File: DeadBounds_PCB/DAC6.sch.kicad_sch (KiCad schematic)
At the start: 0 parts

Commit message: Added 6-bit DAC
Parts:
- added LS1: Speaker, symbol Device:Speaker
- added R1, R2, R3, R4, R5: 12k, symbol Device:R_US
- added R10, R6, R7, R8, R9: 1.5k, symbol Device:R_US
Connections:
- new net: LS1.1, R1.2, R10.2, R3.2, R4.2, R5.2, R6.2, R8.2, R9.2
- new net: R6.1, R7.2
- new net: R1.1, R2.2
- new net DAC6_0: R2.1
- new net DAC6_1: R3.1
- new net DAC6_2: R4.1, R5.1
- new net DAC6_3: R7.1
- new net DAC6_4: R8.1
- new net DAC6_5: R10.1, R9.1
- new net GND: LS1.2

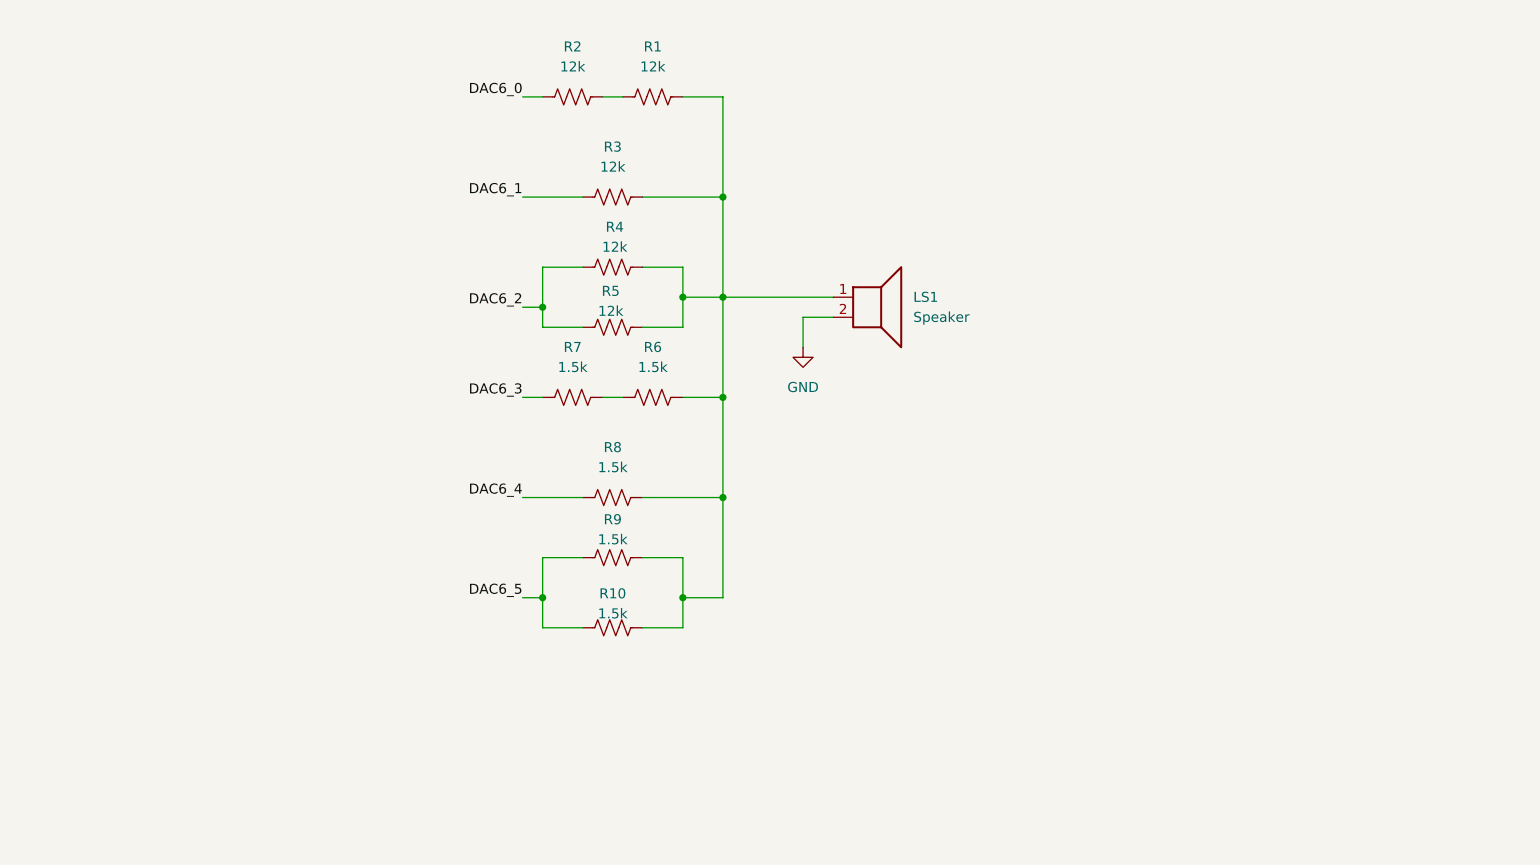
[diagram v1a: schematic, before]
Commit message: Finished schematics, assigned/made footprints except for resistors
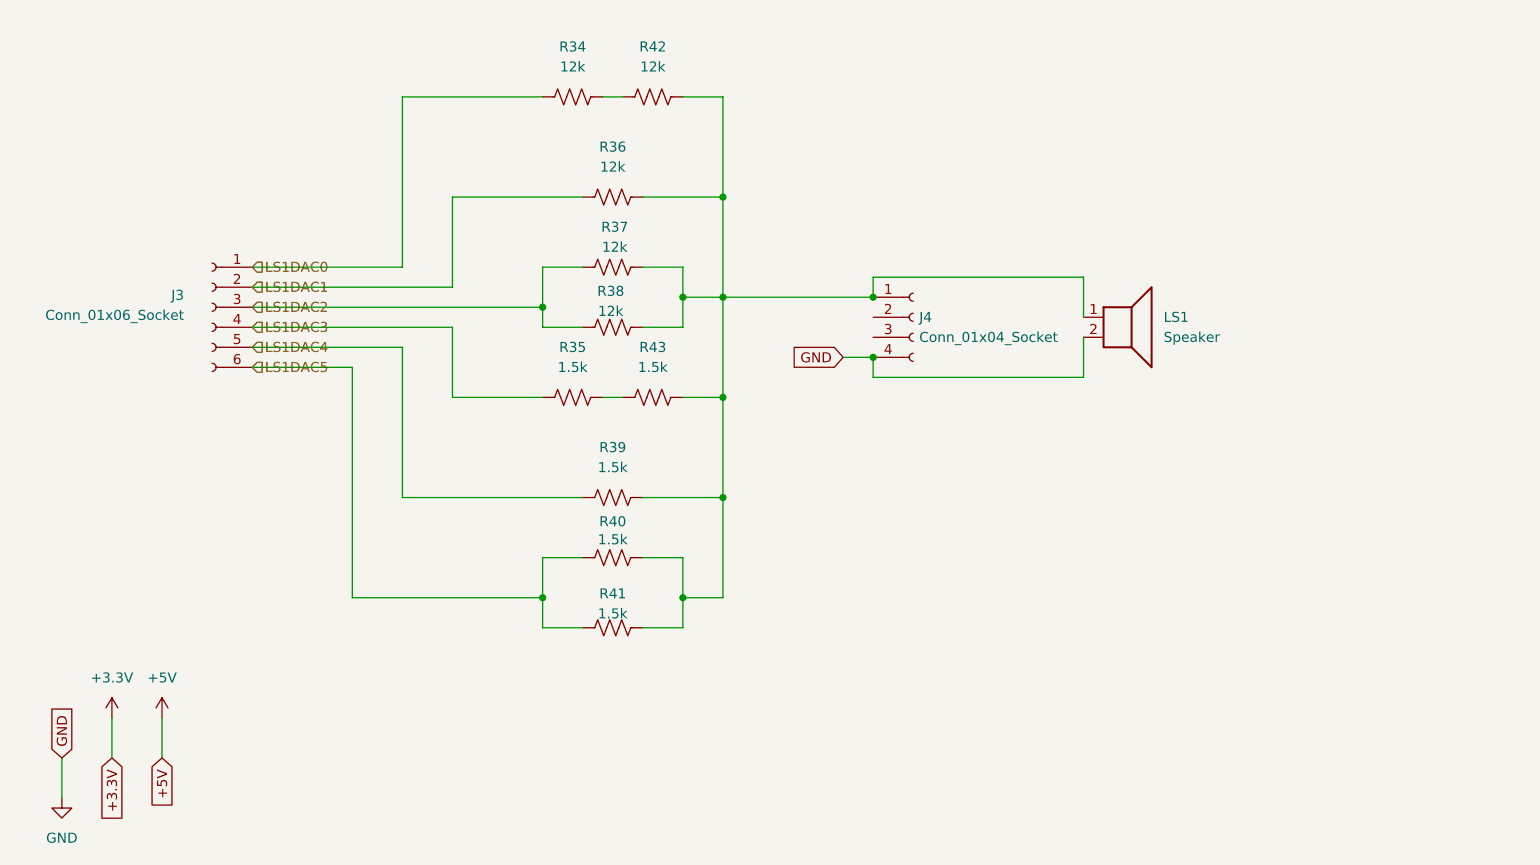
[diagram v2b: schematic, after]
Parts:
- added J3: Conn_01x06_Socket, Connector_PinSocket_2.54mm:PinSocket_1x06_P2.54mm_Horizontal, symbol Connector:Conn_01x06_Socket
- added J4: Conn_01x04_Socket, Connector_PinSocket_2.54mm:PinSocket_1x04_P2.54mm_Horizontal, symbol Connector:Conn_01x04_Socket
- renumbered R2 to R34, R7 to R35, R3 to R36, R4 to R37, R5 to R38, R8 to R39, R9 to R40, R10 to R41, R1 to R42, R6 to R43
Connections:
- net GND: now also J4.4 (Pin_4)
- net at LS1.1, R36.2, R37.2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: now also J4.1 (Pin_1)
- net DAC6_0 renamed LS1DAC0
- net LS1DAC0: now also J3.1 (Pin_1)
- net DAC6_1 renamed LS1DAC1
- net LS1DAC1: now also J3.2 (Pin_2)
- net DAC6_2 renamed LS1DAC2
- net LS1DAC2: now also J3.3 (Pin_3)
- net DAC6_3 renamed LS1DAC3
- net LS1DAC3: now also J3.4 (Pin_4)
- net DAC6_4 renamed LS1DAC4
- net LS1DAC4: now also J3.5 (Pin_5)
- net DAC6_5 renamed LS1DAC5
- net LS1DAC5: now also J3.6 (Pin_6)

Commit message: MCU wiring and LED resistance edits
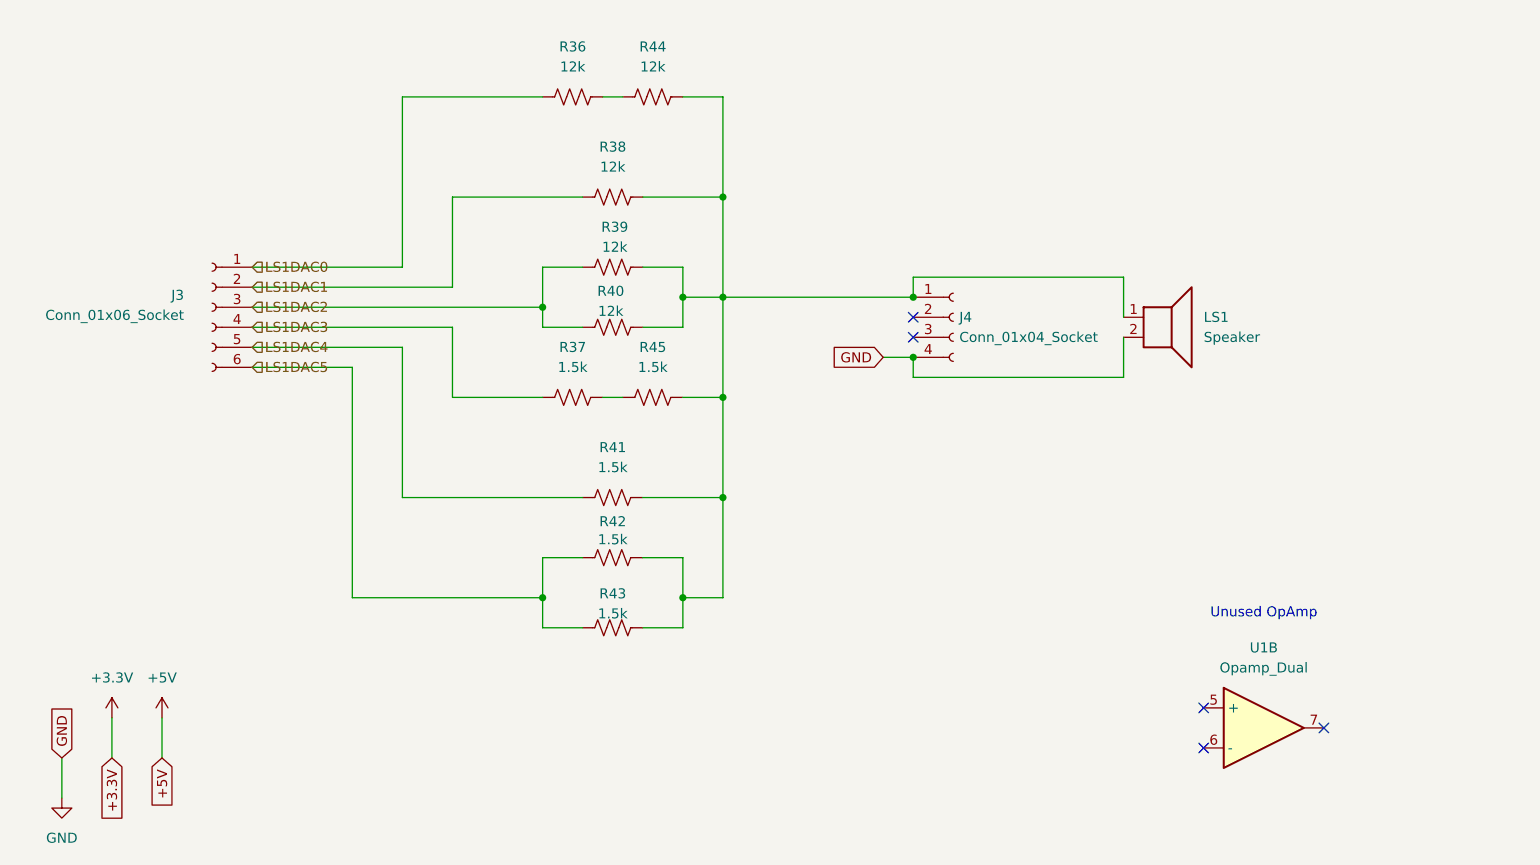
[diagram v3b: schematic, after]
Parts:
- added U1: Opamp_Dual, symbol Device:Opamp_Dual
- R36: renamed from R34; footprint (none) -> Resistor_THT:R_Axial_DIN0207_L6.3mm_D2.5mm_P7.62mm_Horizontal
- R37: renamed from R35; footprint (none) -> Resistor_THT:R_Axial_DIN0207_L6.3mm_D2.5mm_P7.62mm_Horizontal
- R38: renamed from R36; footprint (none) -> Resistor_THT:R_Axial_DIN0207_L6.3mm_D2.5mm_P7.62mm_Horizontal
- R39: renamed from R37; footprint (none) -> Resistor_THT:R_Axial_DIN0207_L6.3mm_D2.5mm_P7.62mm_Horizontal
- R40: renamed from R38; footprint (none) -> Resistor_THT:R_Axial_DIN0207_L6.3mm_D2.5mm_P7.62mm_Horizontal
- R41: renamed from R39; footprint (none) -> Resistor_THT:R_Axial_DIN0207_L6.3mm_D2.5mm_P7.62mm_Horizontal
- R42: renamed from R40; footprint (none) -> Resistor_THT:R_Axial_DIN0207_L6.3mm_D2.5mm_P7.62mm_Horizontal
- R43: renamed from R41; footprint (none) -> Resistor_THT:R_Axial_DIN0207_L6.3mm_D2.5mm_P7.62mm_Horizontal
- R44: renamed from R42; footprint (none) -> Resistor_THT:R_Axial_DIN0207_L6.3mm_D2.5mm_P7.62mm_Horizontal
- R45: renamed from R43; footprint (none) -> Resistor_THT:R_Axial_DIN0207_L6.3mm_D2.5mm_P7.62mm_Horizontal
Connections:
- no-connect marks 0 -> 5
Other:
- note added: "Unused OpAmp"

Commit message: Added footprints, made PCB. Basically done(?)
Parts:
- removed U1: Opamp_Dual, symbol Device:Opamp_Dual
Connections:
- no-connect marks 5 -> 2
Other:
- note removed: "Unused OpAmp"
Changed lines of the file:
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@@
 	(generator_version "10.0")
 	(paper "A4")
-	(text "Unused OpAmp\n\n"
-		(exclude_from_sim no)
-		(at 223.52 130.048 0)
-		(effects
-			(font
-				(size 1.27 1.27)
-			)
-		)
-	)
 	(junction
 		(at 154.94 88.9)
@@
 		(diameter 0)
 		(color 0 0 0 0)
-	)
-	(no_connect
-		(at 215.9 140.97)
-	)
-	(no_connect
-		(at 231.14 143.51)
-	)
-	(no_connect
-		(at 215.9 146.05)
 	)
 	(no_connect
@@
 				)
 			)
-		)
-	)
-	(symbol
-		(lib_id "Device:Opamp_Dual")
-		(at 223.52 143.51 0)
-		(unit 2)
-		(body_style 1)
-		(exclude_from_sim no)
-		(in_bom yes)
-		(on_board yes)
-		(in_pos_files yes)
-		(dnp no)
-		(fields_autoplaced yes)
-		(property "Reference" "U1"
-			(at 223.52 133.35 0)
-			(show_name no)
-			(do_not_autoplace no)
-			(effects
-				(font
-					(size 1.27 1.27)
-				)
-			)
-		)
-		(property "Value" "Opamp_Dual"
-			(at 223.52 135.89 0)
-			(show_name no)
-			(do_not_autoplace no)
-			(effects
-				(font
-					(size 1.27 1.27)
-				)
-			)
-		)
-		(property "Footprint" ""
-			(at 223.52 143.51 0)
-			(hide yes)
-			(show_name no)
-			(do_not_autoplace no)
-			(effects
-				(font
-					(size 1.27 1.27)
-				)
-			)
-		)
-		(property "Datasheet" ""
-			(at 223.52 143.51 0)
-			(hide yes)
-			(show_name no)
-			(do_not_autoplace no)
-			(effects
-				(font
-					(size 1.27 1.27)
-				)
-			)
-		)
-		(property "Description" "Dual operational amplifier"
-			(at 223.52 143.51 0)
-			(hide yes)
-			(show_name no)
-			(do_not_autoplace no)
-			(effects
-				(font
-					(size 1.27 1.27)
-				)
-			)
-		)
-		(property "Sim.Library" "${KICAD9_SYMBOL_DIR}/Simulation_SPICE.sp"
-			(at 223.52 143.51 0)
-			(hide yes)
-			(show_name no)
-			(do_not_autoplace no)
-			(effects
-				(font
-					(size 1.27 1.27)
-				)
-			)
-		)
-		(property "Sim.Name" "kicad_builtin_opamp_dual"
-			(at 223.52 143.51 0)
-			(hide yes)
-			(show_name no)
-			(do_not_autoplace no)
-			(effects
-				(font
-					(size 1.27 1.27)
-				)
-			)
-		)
-		(property "Sim.Device" "SUBCKT"
-			(at 223.52 143.51 0)
-			(hide yes)
-			(show_name no)
-			(do_not_autoplace no)
-			(effects
-				(font
-					(size 1.27 1.27)
-				)
-			)
-		)
-		(property "Sim.Pins" "1=out1 2=in1- 3=in1+ 4=vee 5=in2+ 6=in2- 7=out2 8=vcc"
-			(at 223.52 143.51 0)
-			(hide yes)
-			(show_name no)
-			(do_not_autoplace no)
-			(effects
-				(font
-					(size 1.27 1.27)
-				)
-			)
-		)
-		(pin "8"
-		)
-		(pin "5"
-		)
-		(pin "4"
-		)
-		(pin "2"
-		)
-		(pin "6"
-		)
-		(pin "7"
-		)
-		(pin "1"
-		)
-		(pin "3"
-		)
-		(instances
-			(project "DeadBounds_PCB"
-				(path "/c652495f-dd42-4f45-9891-1e05b67942c0/8be2fbc8-3e56-4fbf-8c37-1c5635a7d56d"
-					(reference "U1")
-					(unit 2)
-				)
-			)

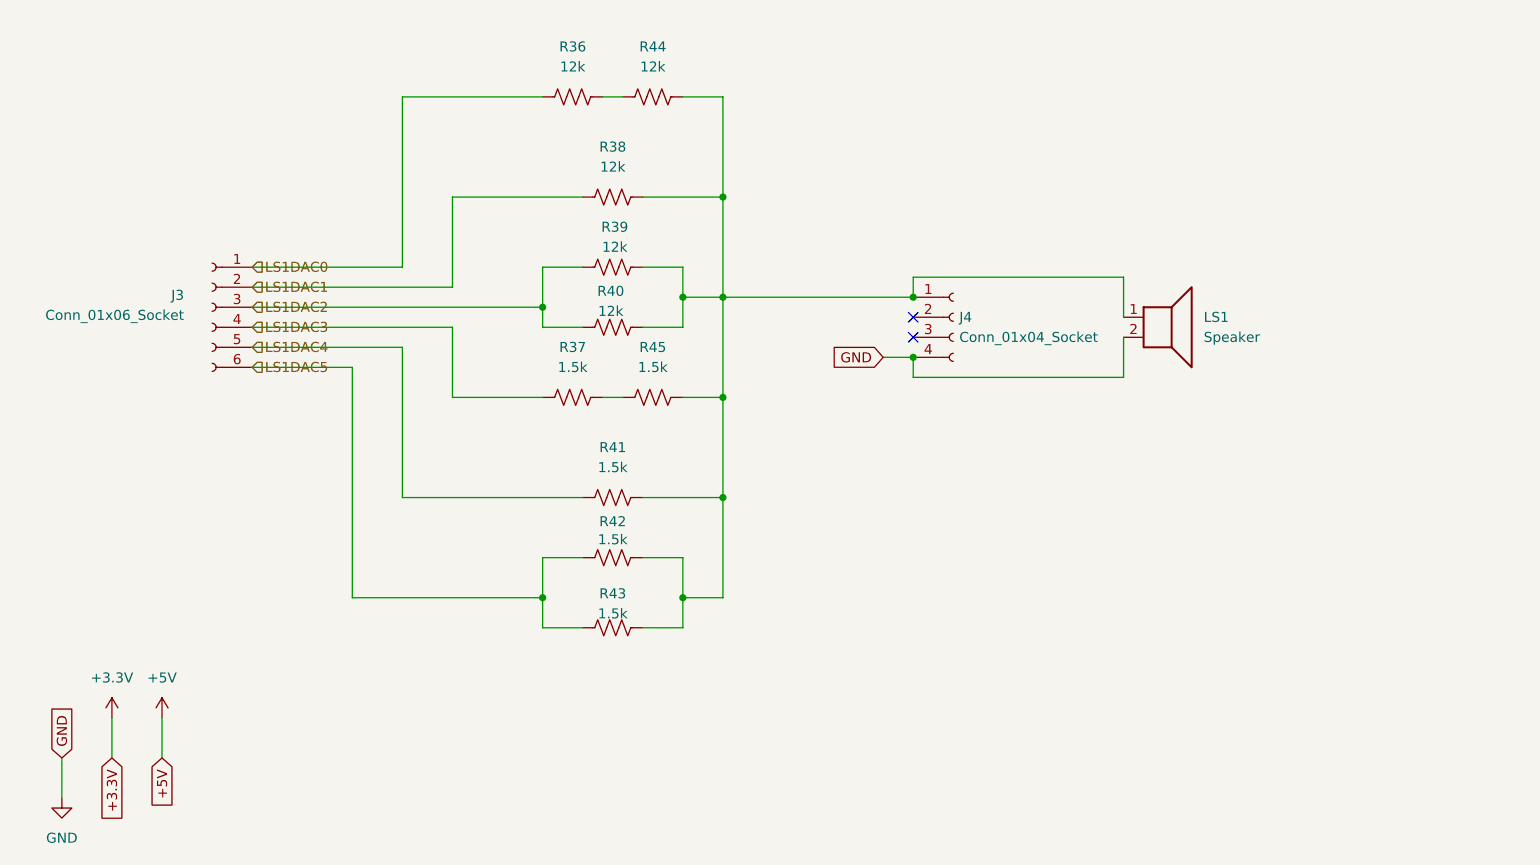
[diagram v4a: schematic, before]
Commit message: Added amplifier circuit and additional jumpers to PCB
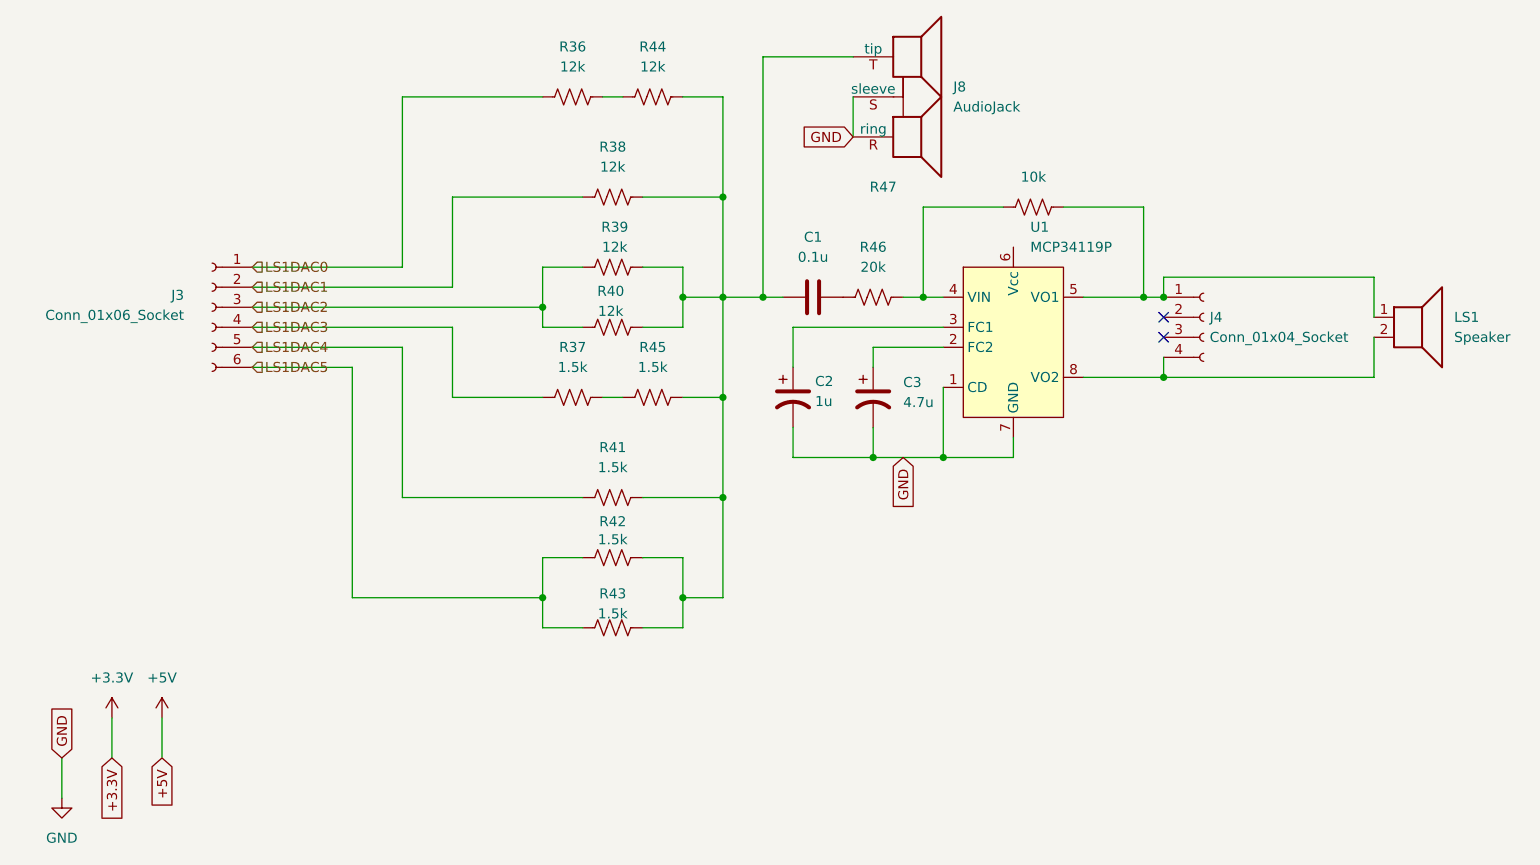
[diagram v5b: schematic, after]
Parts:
- added C1: 0.1u, ECE319K:C_Axial_200mil, symbol DeadBounds_Symbols:C
- added C2: 1u, ECE319K:CP_Radial_Tantal200mil, symbol DeadBounds_Symbols:C_Polarized
- added C3: 4.7u, ECE319K:CP_Radial_Tantal200mil, symbol DeadBounds_Symbols:C_Polarized
- added J8: AudioJack, ECE319K:Jack_3.5mm_CUI_SJ1-3523N_Horizontal, symbol DeadBounds_Symbols:HeadphoneJack
- added R46: 20k, Resistor_THT:R_Axial_DIN0207_L6.3mm_D2.5mm_P7.62mm_Horizontal, symbol Device:R_US
- added R47: 10k, Resistor_THT:R_Axial_DIN0207_L6.3mm_D2.5mm_P7.62mm_Horizontal, symbol Device:R_US
- added U1: MCP34119P, ECE319K:DIP-8_W7.62mm_LongPads, symbol DeadBounds_Symbols:MCP34119P
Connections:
- net GND: now also C2.2, C3.2, J8.R (ring), J8.S (sleeve), U1.1 (CD), U1.7 (GND); no longer J4.4 (Pin_4), LS1.2
- net at R38.2, R39.2, R40.2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: now also C1.2, J8.T (tip); no longer J4.1 (Pin_1), LS1.1
- new net: C1.1, R46.1
- new net: C2.1, U1.3 (FC1)
- new net: J4.1 (Pin_1), LS1.1, R47.1, U1.5 (VO1)
- new net: J4.4 (Pin_4), LS1.2, U1.8 (VO2)
- new net: R46.2, R47.2, U1.4 (VIN)
- new net: C3.1, U1.2 (FC2)

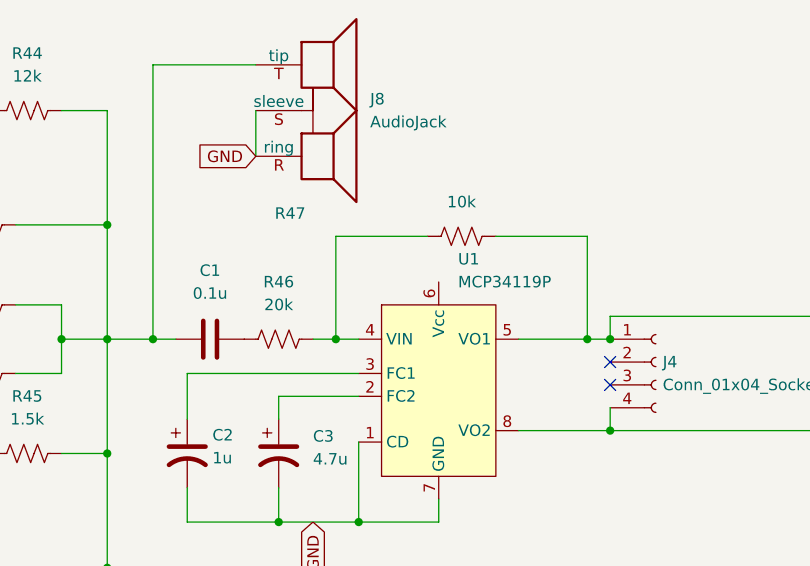
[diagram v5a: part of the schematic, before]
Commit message: Added mounting holes and rerouted around joystick. PCB Ordered
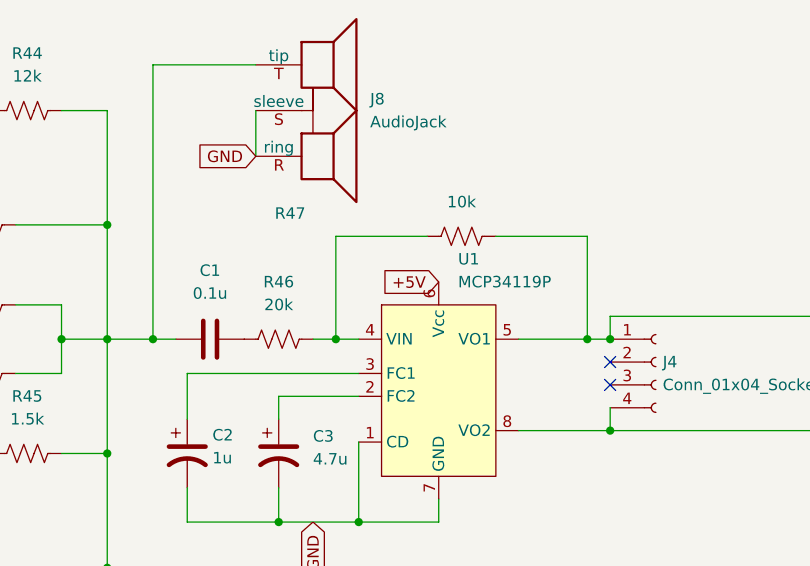
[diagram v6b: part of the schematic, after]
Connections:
- net +5V: now also U1.6 (Vcc)
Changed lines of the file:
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@@
+		)
+	)
+	(global_label "+5V"
+		(shape input)
+		(at 191.77 82.55 180)
+		(fields_autoplaced yes)
+		(effects
+			(font
+				(size 1.27 1.27)
+			)
+			(justify right)
+		)
+		(property "Intersheetrefs" "${INTERSHEET_REFS}"
+			(at 184.9143 82.55 0)
+			(hide yes)
+			(show_name no)
+			(do_not_autoplace no)
+			(effects
+				(font
+					(size 1.27 1.27)
+				)
+				(justify right)
+			)
 		)
 	)
